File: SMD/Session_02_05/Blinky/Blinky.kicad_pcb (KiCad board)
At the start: 2 copper layers, 30 x 30 mm, 12 parts, among them U1 TLC551CD‎

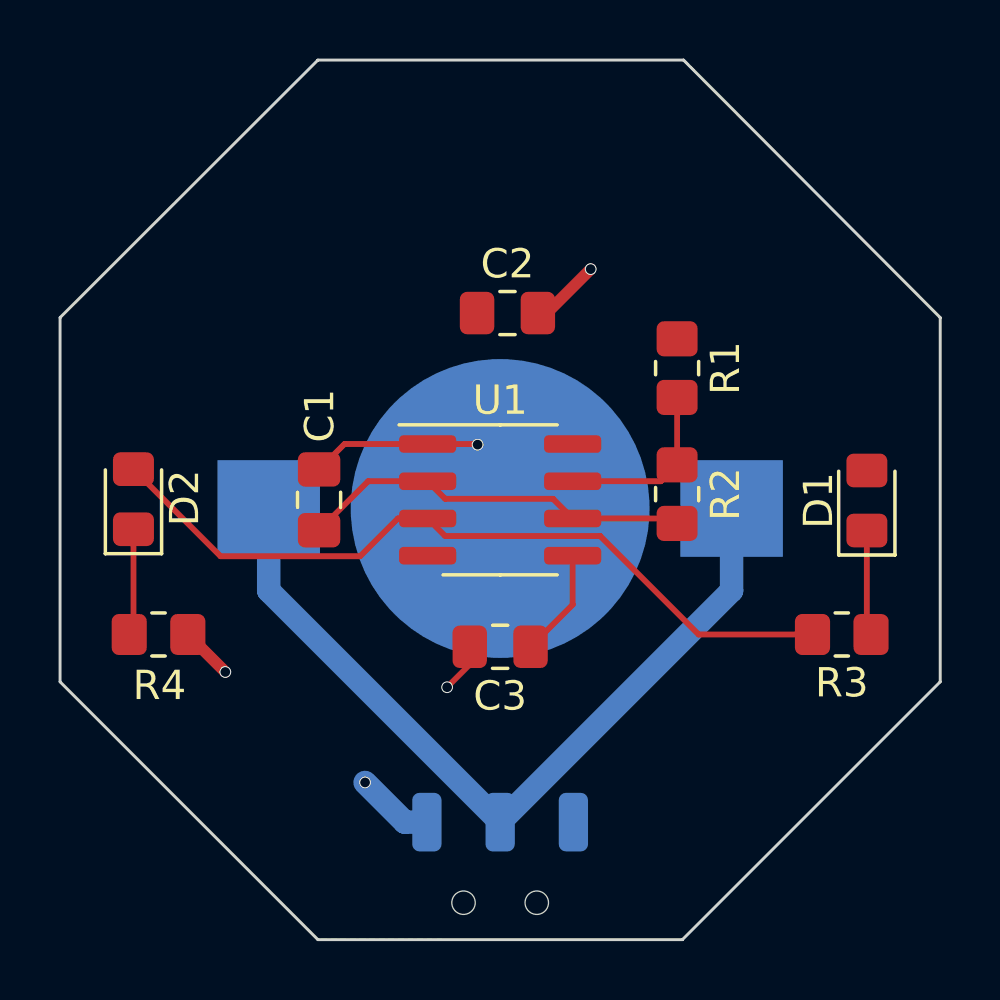
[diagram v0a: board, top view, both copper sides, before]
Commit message: Makes corrections to the design rules
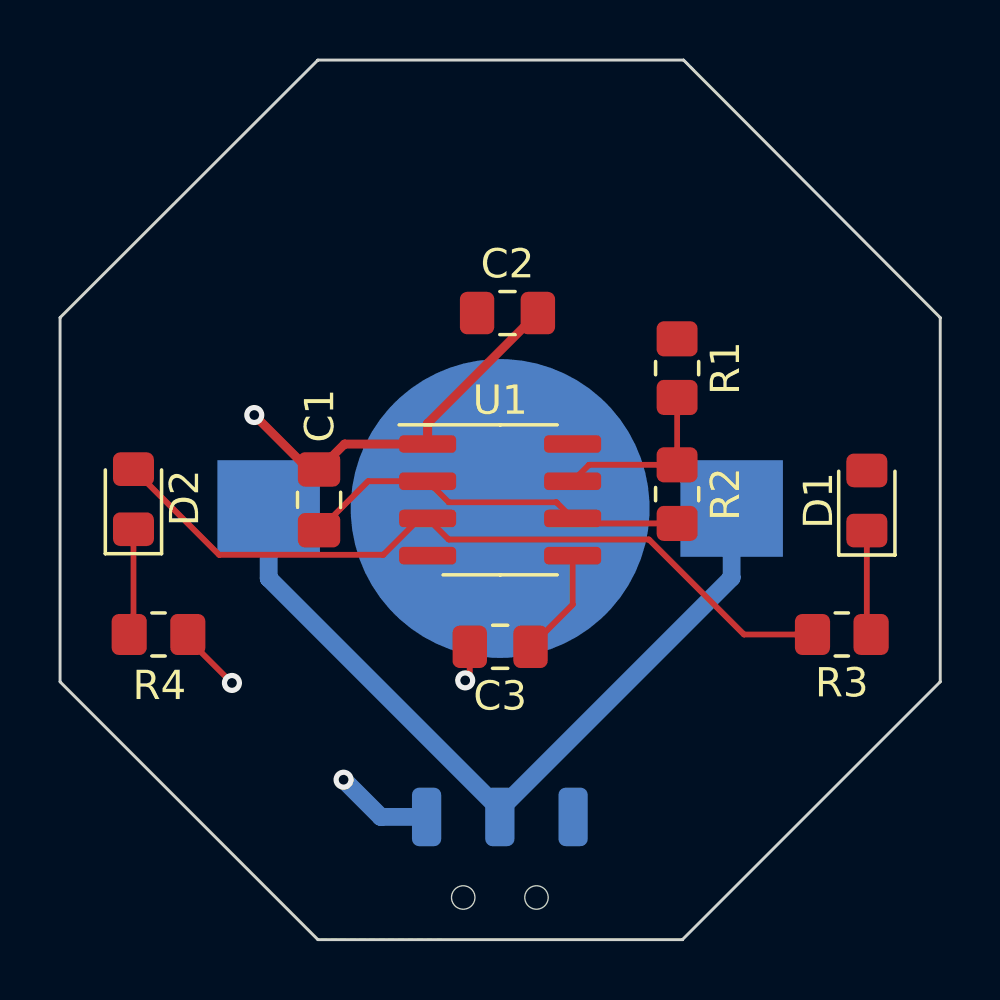
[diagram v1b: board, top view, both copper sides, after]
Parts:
- moved SW? 0.18 mm to (193.0, 64.5)
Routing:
- net GND: track 11.7 -> 16.6 mm, vias 4 -> 3
- net /VCC: track 2.67 -> 3.36 mm
- net Net-(BT1-Pad1): track 28.0 -> 27.3 mm
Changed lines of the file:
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@@
     (48 "B.Fab" user)
     (49 "F.Fab" user)
-    (50 "User.1" user)
-    (51 "User.2" user)
-    (52 "User.3" user)
-    (53 "User.4" user)
-    (54 "User.5" user)
-    (55 "User.6" user)
-    (56 "User.7" user)
-    (57 "User.8" user)
-    (58 "User.9" user)
+    (50 "User.1" user "Nutzer.1")
+    (51 "User.2" user "Nutzer.2")
+    (52 "User.3" user "Nutzer.3")
+    (53 "User.4" user "Nutzer.4")
+    (54 "User.5" user "Nutzer.5")
+    (55 "User.6" user "Nutzer.6")
+    (56 "User.7" user "Nutzer.7")
+    (57 "User.8" user "Nutzer.8")
+    (58 "User.9" user "Nutzer.9")
   )
   (setup
@@
   )
   (footprint "Blinky_ZAM:SSK-1202" (layer "B.Cu")
-    (at 193.05 64.6944)
+    (at 193.040001 64.516401)
     (property "Datasheet" "~")
     (property "Reference" "SW?")
@@
       (effects (font (size 1 1) (thickness 0.15)) (justify mirror))
     )
-    (fp_rect (start -3.500001 1) (end 3.500001 4) (layer "B.SilkS") (width 0.1524) (fill none))
     (fp_rect (start -2 5.499999) (end -0.5 4) (layer "B.SilkS") (width 0.1524) (fill none))
+    (fp_rect (start -3.500001 1.1) (end 3.5 4) (layer "B.SilkS") (width 0.1524) (fill none))
     (fp_rect (start -3.5 5.5) (end 3.5 -1) (layer "B.CrtYd") (width 0.01) (fill none))
     (pad "" np_thru_hole circle (at -1.25 2.75) (size 0.8 0.8) (drill 0.8) (layers F&B.Cu *.Mask))
@@
       (xy 199.31 38.685)
     ) (layer "Edge.Cuts") (width 0.1) (fill none))
-  (segment (start 193.05 64.6944) (end 185.15 56.7944) (width 0.8) (layer "B.Cu") (net 1))
-  (segment (start 193.05 64.6944) (end 200.95 56.7944) (width 0.8) (layer "B.Cu") (net 1))
-  (segment (start 200.95 56.7944) (end 200.95 53.99) (width 0.8) (layer "B.Cu") (net 1))
-  (segment (start 185.15 56.7944) (end 185.15 53.99) (width 0.8) (layer "B.Cu") (net 1))
-  (segment (start 194.3375 47.32) (end 194.64 47.32) (width 0.4) (layer "F.Cu") (net 2))
-  (segment (start 192.0125 58.71) (end 192.0125 59.3175) (width 0.2) (layer "F.Cu") (net 2))
-  (segment (start 192.0125 59.3175) (end 191.24 60.09) (width 0.2) (layer "F.Cu") (net 2))
-  (segment (start 192.26 51.79) (end 192.28 51.81) (width 0.2) (layer "F.Cu") (net 2))
-  (segment (start 194.64 47.32) (end 196.14 45.82) (width 0.4) (layer "F.Cu") (net 2))
-  (segment (start 182.39 58.29) (end 183.67 59.57) (width 0.4) (layer "F.Cu") (net 2))
-  (segment (start 187.7375 51.79) (end 190.575 51.79) (width 0.2) (layer "F.Cu") (net 2))
-  (segment (start 190.575 51.79) (end 192.26 51.79) (width 0.2) (layer "F.Cu") (net 2))
-  (segment (start 186.87 52.6575) (end 187.7375 51.79) (width 0.2) (layer "F.Cu") (net 2))
-  (via (at 192.28 51.81) (size 0.4) (drill 0.3302) (layers "F.Cu" "B.Cu") (net 2))
-  (via (at 183.67 59.57) (size 0.4) (drill 0.3302) (layers "F.Cu" "B.Cu") (net 2))
-  (via (at 196.14 45.82) (size 0.4) (drill 0.3302) (layers "F.Cu" "B.Cu") (net 2))
-  (via (at 191.24 60.09) (size 0.4) (drill 0.3302) (layers "F.Cu" "B.Cu") (net 2))
-  (segment (start 190.575 53.06) (end 188.5425 53.06) (width 0.2) (layer "F.Cu") (net 3))
-  (segment (start 198.92 54.33) (end 199.09 54.5) (width 0.2) (layer "F.Cu") (net 3))
-  (segment (start 190.575 53.06) (end 191.17452 53.65952) (width 0.2) (layer "F.Cu") (net 3))
-  (segment (start 194.85452 53.65952) (end 195.525 54.33) (width 0.2) (layer "F.Cu") (net 3))
-  (segment (start 188.5425 53.06) (end 186.87 54.7325) (width 0.2) (layer "F.Cu") (net 3))
-  (segment (start 191.17452 53.65952) (end 194.85452 53.65952) (width 0.2) (layer "F.Cu") (net 3))
-  (segment (start 195.525 54.33) (end 198.92 54.33) (width 0.2) (layer "F.Cu") (net 3))
-  (via (at 188.44 63.34) (size 0.4) (drill 0.3302) (layers "F.Cu" "B.Cu") (net 4))
-  (segment (start 189.7944 64.6944) (end 188.44 63.34) (width 0.8) (layer "B.Cu") (net 4))
-  (segment (start 190.55 64.6944) (end 189.7944 64.6944) (width 0.8) (layer "B.Cu") (net 4))
+  (segment (start 193.04 64.262) (end 185.15 56.372) (width 0.6096) (layer "B.Cu") (net 1))
+  (segment (start 193.04 64.262) (end 200.95 56.352) (width 0.6096) (layer "B.Cu") (net 1))
+  (segment (start 193.04 64.262) (end 193.040001 64.516401) (width 0.2) (layer "B.Cu") (net 1))
+  (segment (start 185.15 56.372) (end 185.15 53.99) (width 0.6096) (layer "B.Cu") (net 1))
+  (segment (start 200.95 56.352) (end 200.95 53.99) (width 0.6096) (layer "B.Cu") (net 1))
+  (segment (start 190.575 51.79) (end 190.575 51.0825) (width 0.3048) (layer "F.Cu") (net 2))
+  (segment (start 186.5155 52.6575) (end 184.658 50.8) (width 0.3048) (layer "F.Cu") (net 2))
+  (segment (start 192.0125 58.71) (end 192.0125 59.7015) (width 0.2) (layer "F.Cu") (net 2))
+  (segment (start 186.87 52.6575) (end 186.5155 52.6575) (width 0.3048) (layer "F.Cu") (net 2))
+  (segment (start 187.7375 51.79) (end 186.87 52.6575) (width 0.3048) (layer "F.Cu") (net 2))
+  (segment (start 182.39 58.438) (end 183.896 59.944) (width 0.2) (layer "F.Cu") (net 2))
+  (segment (start 182.39 58.29) (end 182.39 58.438) (width 0.2) (layer "F.Cu") (net 2))
+  (segment (start 190.575 51.0825) (end 194.3375 47.32) (width 0.3048) (layer "F.Cu") (net 2))
+  (segment (start 192.0125 59.7015) (end 191.857588 59.856412) (width 0.2) (layer "F.Cu") (net 2))
+  (segment (start 190.575 51.79) (end 187.7375 51.79) (width 0.3048) (layer "F.Cu") (net 2))
+  (via (at 191.857588 59.856412) (size 0.6858) (drill 0.3302) (layers "F.Cu" "B.Cu") (net 2))
+  (via (at 183.896 59.944) (size 0.6858) (drill 0.3302) (layers "F.Cu" "B.Cu") (net 2))
+  (via (at 184.658 50.8) (size 0.6858) (drill 0.3302) (layers "F.Cu" "B.Cu") (net 2))
+  (segment (start 199.09 54.5) (end 195.695 54.5) (width 0.2) (layer "F.Cu") (net 3))
+  (segment (start 188.5425 53.06) (end 190.575 53.06) (width 0.2) (layer "F.Cu") (net 3))
+  (segment (start 195.695 54.5) (end 195.525 54.33) (width 0.2) (layer "F.Cu") (net 3))
+  (segment (start 186.87 54.7325) (end 188.5425 53.06) (width 0.2) (layer "F.Cu") (net 3))
+  (segment (start 195.525 54.33) (end 194.97308 53.77808) (width 0.2) (layer "F.Cu") (net 3))
+  (segment (start 191.29308 53.77808) (end 190.575 53.06) (width 0.2) (layer "F.Cu") (net 3))
+  (segment (start 194.97308 53.77808) (end 191.29308 53.77808) (width 0.2) (layer "F.Cu") (net 3))
+  (via (at 187.706 63.246) (size 0.6858) (drill 0.3302) (layers "F.Cu" "B.Cu") (net 4))
+  (segment (start 190.540001 64.516401) (end 188.976401 64.516401) (width 0.6096) (layer "B.Cu") (net 4))
+  (segment (start 188.976401 64.516401) (end 187.706 63.246) (width 0.6096) (layer "B.Cu") (net 4))
   (segment (start 194.0875 58.71) (end 195.525 57.2725) (width 0.2) (layer "F.Cu") (net 5))
   (segment (start 195.525 57.2725) (end 195.525 55.6) (width 0.2) (layer "F.Cu") (net 5))
@@
   (segment (start 180.535 58.145) (end 180.535 54.6975) (width 0.2) (layer "F.Cu") (net 7))
   (segment (start 180.39 58.29) (end 180.535 58.145) (width 0.2) (layer "F.Cu") (net 7))
-  (segment (start 203.71 58.29) (end 199.825717 58.29) (width 0.2) (layer "F.Cu") (net 8))
-  (segment (start 196.465717 54.93) (end 191.175 54.93) (width 0.2) (layer "F.Cu") (net 8))
-  (segment (start 183.50702 55.61952) (end 188.27048 55.61952) (width 0.2) (layer "F.Cu") (net 8))
-  (segment (start 188.27048 55.61952) (end 189.56 54.33) (width 0.2) (layer "F.Cu") (net 8))
-  (segment (start 189.56 54.33) (end 190.575 54.33) (width 0.2) (layer "F.Cu") (net 8))
-  (segment (start 199.825717 58.29) (end 196.465717 54.93) (width 0.2) (layer "F.Cu") (net 8))
-  (segment (start 191.175 54.93) (end 190.575 54.33) (width 0.2) (layer "F.Cu") (net 8))
-  (segment (start 180.535 52.6475) (end 183.50702 55.61952) (width 0.2) (layer "F.Cu") (net 8))
+  (segment (start 201.370178 58.29) (end 203.71 58.29) (width 0.2) (layer "F.Cu") (net 8))
+  (segment (start 183.45942 55.57192) (end 189.05968 55.57192) (width 0.2) (layer "F.Cu") (net 8))
+  (segment (start 190.575 54.33) (end 191.29308 55.04808) (width 0.2) (layer "F.Cu") (net 8))
+  (segment (start 189.05968 55.57192) (end 190.3016 54.33) (width 0.2) (layer "F.Cu") (net 8))
+  (segment (start 198.128258 55.04808) (end 201.370178 58.29) (width 0.2) (layer "F.Cu") (net 8))
+  (segment (start 180.535 52.6475) (end 183.45942 55.57192) (width 0.2) (layer "F.Cu") (net 8))
+  (segment (start 190.3016 54.33) (end 190.575 54.33) (width 0.2) (layer "F.Cu") (net 8))
+  (segment (start 191.29308 55.04808) (end 198.128258 55.04808) (width 0.2) (layer "F.Cu") (net 8))
+  (segment (start 196.085 52.5) (end 195.525 53.06) (width 0.2) (layer "F.Cu") (net 9))
   (segment (start 199.09 50.2) (end 199.09 52.5) (width 0.2) (layer "F.Cu") (net 9))
-  (segment (start 198.53 53.06) (end 195.525 53.06) (width 0.2) (layer "F.Cu") (net 9))
-  (segment (start 199.09 52.5) (end 198.53 53.06) (width 0.2) (layer "F.Cu") (net 9))
+  (segment (start 199.09 52.5) (end 196.085 52.5) (width 0.2) (layer "F.Cu") (net 9))
   (zone (net 4) (net_name "/VCC") (layer "F.Cu") (hatch edge 0.508)
     (connect_pads (clearance 0.1524))

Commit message: Corrections to the switch footprint
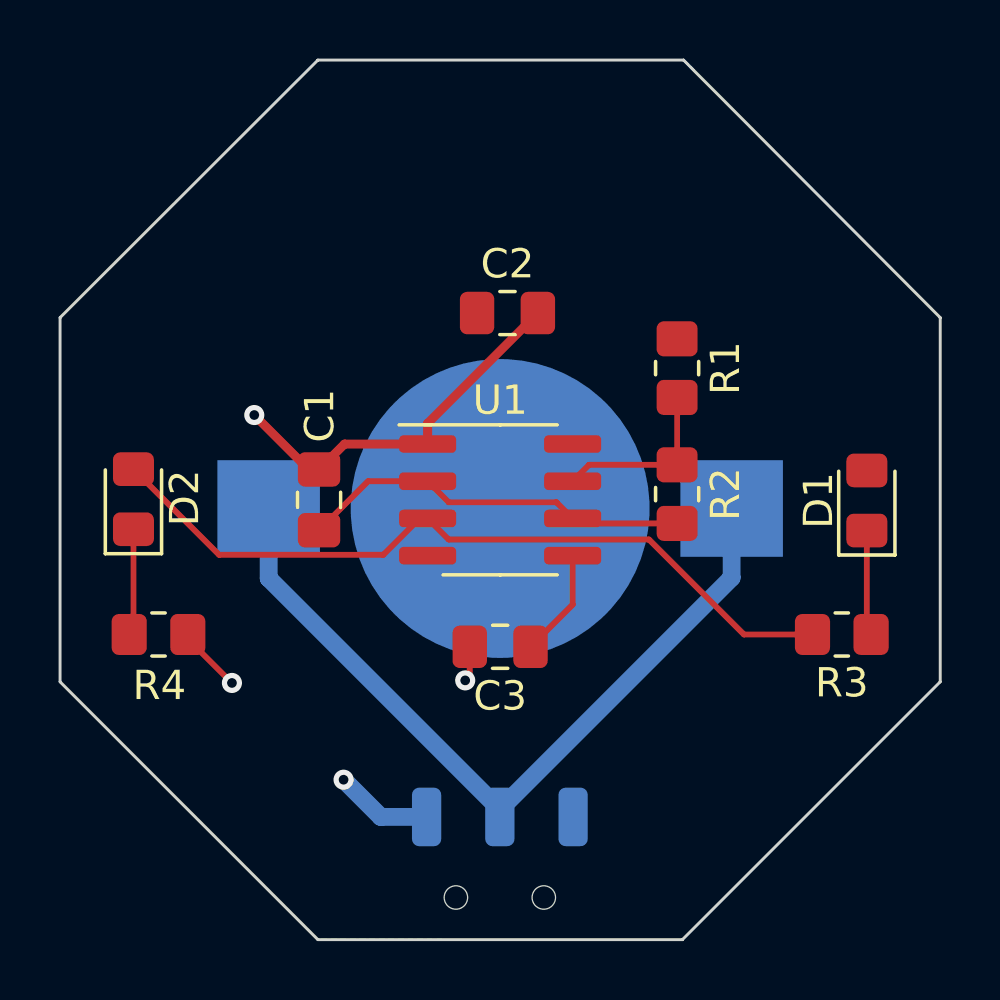
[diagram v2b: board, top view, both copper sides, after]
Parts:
- turned BT1 to 0 degrees
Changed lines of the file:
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@@
       (effects (font (size 1 1) (thickness 0.15)) (justify mirror))
     )
+    (fp_rect (start -3.500001 1.1) (end 3.500001 4) (layer "B.SilkS") (width 0.1524) (fill none))
     (fp_rect (start -2 5.499999) (end -0.5 4) (layer "B.SilkS") (width 0.1524) (fill none))
-    (fp_rect (start -3.500001 1.1) (end 3.5 4) (layer "B.SilkS") (width 0.1524) (fill none))
     (fp_rect (start -3.5 5.5) (end 3.5 -1) (layer "B.CrtYd") (width 0.01) (fill none))
-    (pad "" np_thru_hole circle (at -1.25 2.75) (size 0.8 0.8) (drill 0.8) (layers F&B.Cu *.Mask))
-    (pad "" np_thru_hole circle (at 1.25 2.75) (size 0.8 0.8) (drill 0.8) (layers F&B.Cu *.Mask))
+    (pad "" np_thru_hole circle (at -1.5 2.75) (size 0.8 0.8) (drill 0.8) (layers F&B.Cu *.Mask))
+    (pad "" np_thru_hole circle (at 1.5 2.75) (size 0.8 0.8) (drill 0.8) (layers F&B.Cu *.Mask))
     (pad "1" smd roundrect (at -2.5 0) (size 1 2) (layers "B.Cu" "B.Paste" "B.Mask") (roundrect_rratio 0.25)
       (net 4 "/VCC") (pinfunction "A") (pintype "passive"))
@@
   )
   (footprint "Battery:BatteryHolder_Keystone_3000_1x12mm" (layer "B.Cu")
-    (at 193.05 53.99 180)
+    (at 193.05 53.99)
     (descr "http://www.keyelco.com/product-pdf.cfm?p=777")
     (tags "Keystone type 3000 coin cell retainer")
@@
     (fp_arc (start -5.378013 -5.447558) (mid -4.942443 -5.378013) (end -4.6 -5.1) (layer "B.Fab") (width 0.1))
     (fp_arc (start 5.3 -5.45) (mid 6.239949 -5.019238) (end 6.6 -4.05) (layer "B.Fab") (width 0.1))
-    (pad "1" smd rect (at 7.9 0 180) (size 3.5 3.3) (layers "B.Cu" "B.Paste" "B.Mask")
+    (pad "1" smd rect (at 7.9 0) (size 3.5 3.3) (layers "B.Cu" "B.Paste" "B.Mask")
       (net 1 "Net-(BT1-Pad1)") (pinfunction "+") (pintype "passive"))
-    (pad "1" smd rect (at -7.9 0 180) (size 3.5 3.3) (layers "B.Cu" "B.Paste" "B.Mask")
+    (pad "1" smd rect (at -7.9 0) (size 3.5 3.3) (layers "B.Cu" "B.Paste" "B.Mask")
       (net 1 "Net-(BT1-Pad1)") (pinfunction "+") (pintype "passive"))
-    (pad "2" smd circle (at 0 0 180) (size 10.2 10.2) (layers "B.Cu" "B.Mask")
+    (pad "2" smd circle (at 0 0) (size 10.2 10.2) (layers "B.Cu" "B.Mask")
       (net 2 "GND") (pinfunction "-") (pintype "passive"))
     (model "${KICAD6_3DMODEL_DIR}/Battery.3dshapes/BatteryHolder_Keystone_3000_1x12mm.wrl"
@@
   (via (at 183.896 59.944) (size 0.6858) (drill 0.3302) (layers "F.Cu" "B.Cu") (net 2))
   (via (at 184.658 50.8) (size 0.6858) (drill 0.3302) (layers "F.Cu" "B.Cu") (net 2))
+  (segment (start 195.525 54.33) (end 194.97308 53.77808) (width 0.2) (layer "F.Cu") (net 3))
   (segment (start 199.09 54.5) (end 195.695 54.5) (width 0.2) (layer "F.Cu") (net 3))
   (segment (start 188.5425 53.06) (end 190.575 53.06) (width 0.2) (layer "F.Cu") (net 3))
   (segment (start 195.695 54.5) (end 195.525 54.33) (width 0.2) (layer "F.Cu") (net 3))
   (segment (start 186.87 54.7325) (end 188.5425 53.06) (width 0.2) (layer "F.Cu") (net 3))
-  (segment (start 195.525 54.33) (end 194.97308 53.77808) (width 0.2) (layer "F.Cu") (net 3))
+  (segment (start 194.97308 53.77808) (end 191.29308 53.77808) (width 0.2) (layer "F.Cu") (net 3))
   (segment (start 191.29308 53.77808) (end 190.575 53.06) (width 0.2) (layer "F.Cu") (net 3))
-  (segment (start 194.97308 53.77808) (end 191.29308 53.77808) (width 0.2) (layer "F.Cu") (net 3))
   (via (at 187.706 63.246) (size 0.6858) (drill 0.3302) (layers "F.Cu" "B.Cu") (net 4))
   (segment (start 190.540001 64.516401) (end 188.976401 64.516401) (width 0.6096) (layer "B.Cu") (net 4))
